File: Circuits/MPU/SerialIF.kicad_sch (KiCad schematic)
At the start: 16 parts, among them U1 ProASIC, U2 ADM3488ARZ, X1 KC2016K50.0000C1GE00

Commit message: MXS interface
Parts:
- added R222: 249, Resistor_SMD:R_0603_1608Metric, symbol QuERI_symbols:Rlowp
- U1: footprint Package_BGA:BGA-484_23.0x23.0mm_Layout22x22_P1.0mm -> Package_BGA:BGA-484_23.0x23.0mm_Layout22x22_P1.0mm
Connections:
- new net: R222.1, U1.P4 (MXAD)
- new net MXAD: R222.2
- new net MXAS: U1.N5 (MXAS)
- new net MXCLK: U1.N6 (MXCLK)
- new net MXDD: U1.M3 (MXDD)
- new net MXDS: U1.M7 (MXDS)

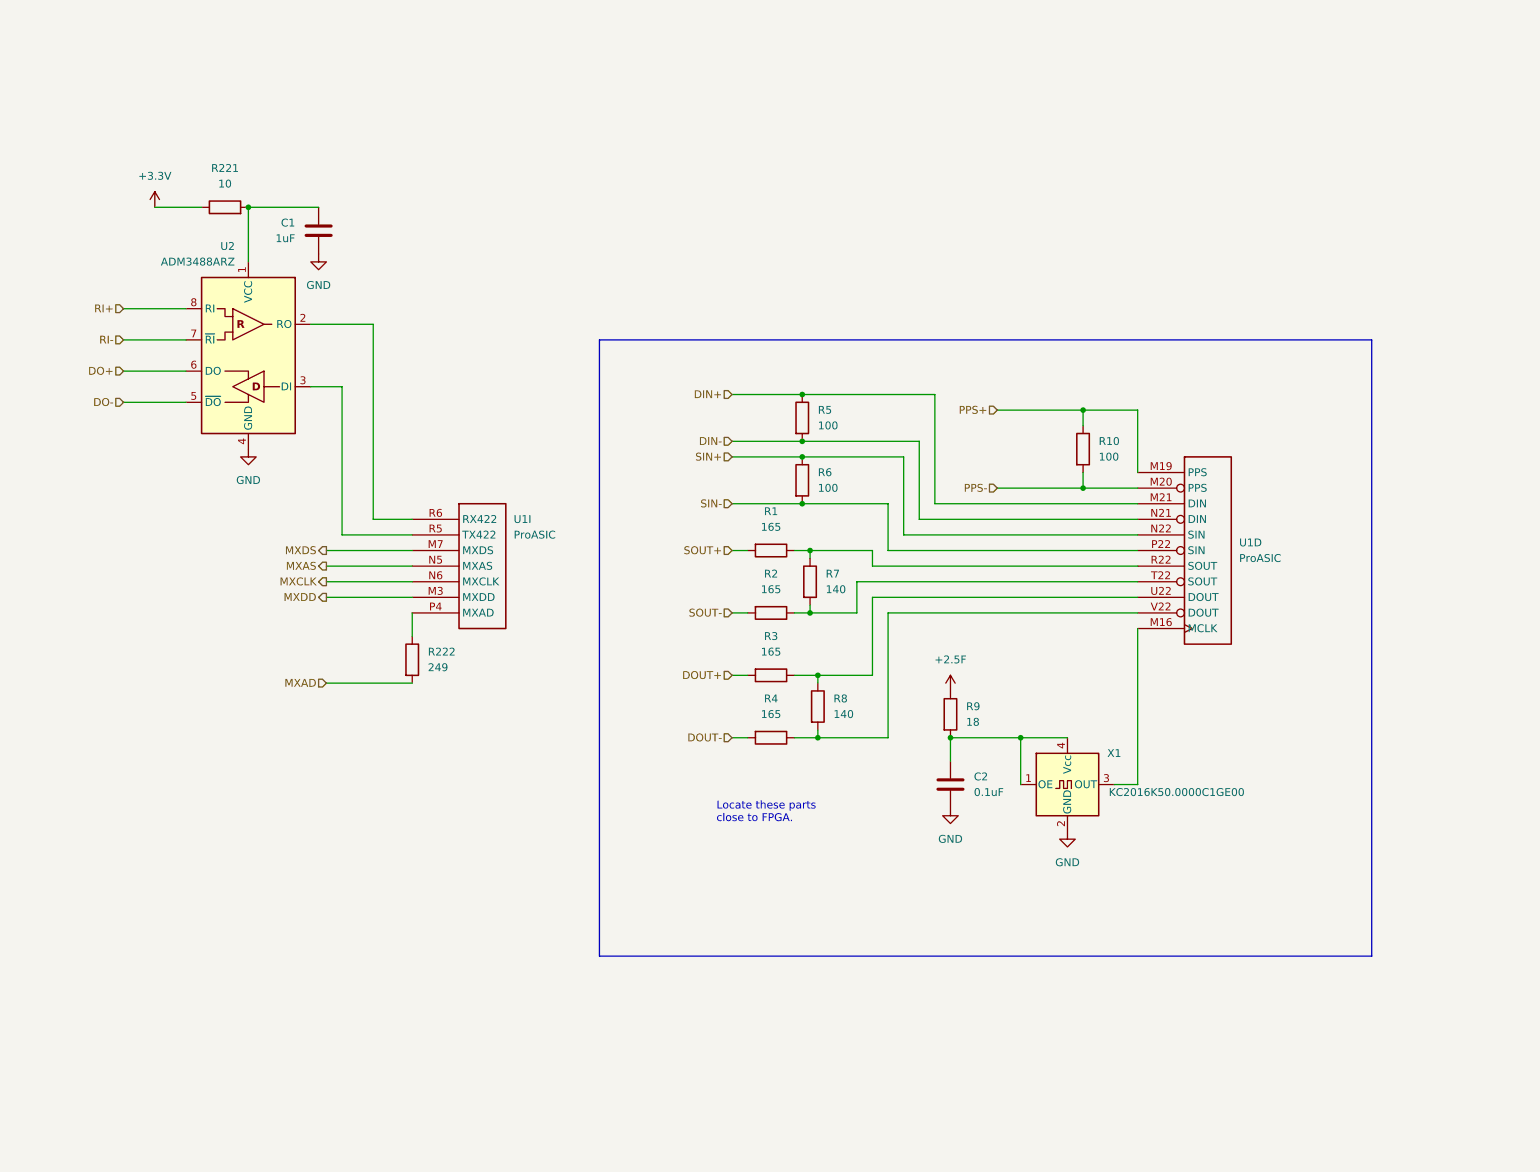
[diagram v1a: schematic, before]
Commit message: LVDS I/F for HV
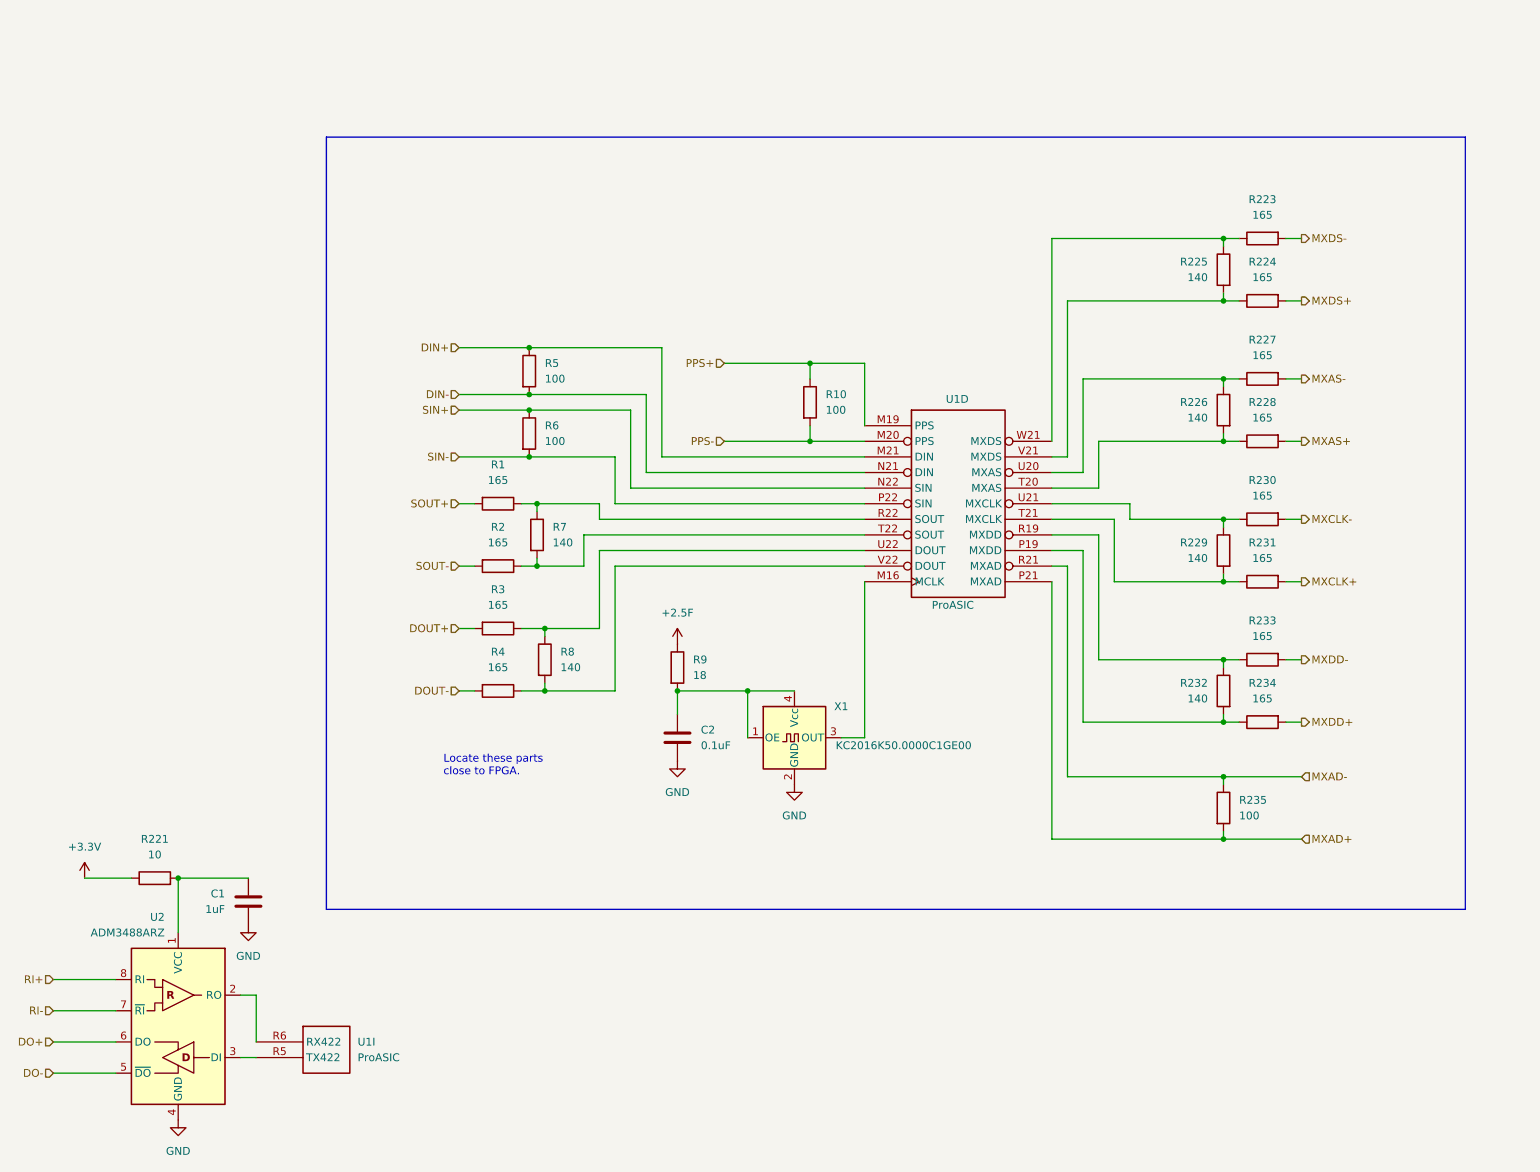
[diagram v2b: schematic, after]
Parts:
- removed R222: 249, Resistor_SMD:R_0603_1608Metric, symbol QuERI_symbols:Rlowp
- added R223, R224, R227, R228, R230, R231, R233, R234: 165, Resistor_SMD:R_0603_1608Metric, symbol QuERI_symbols:Rlowp
- added R225, R226, R229, R232: 140, Resistor_SMD:R_0603_1608Metric, symbol QuERI_symbols:Rlowp
- added R235: 100, Resistor_SMD:R_0603_1608Metric, symbol QuERI_symbols:Rlowp
- U1: desc FPGA -> FPGA; manf# A3PE3000-FGG484 -> A3PE3000-FGG484
- U1: footprint Package_BGA:BGA-484_23.0x23.0mm_Layout22x22_P1.0mm -> Package_BGA:BGA-484_23.0x23.0mm_Layout22x22_P1.0mm; desc FPGA -> FPGA; manf# (none) -> A3PE3000-FGG484
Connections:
- removed net MXAS: U1.N5 (MXAS)
- removed net MXCLK: U1.N6 (MXCLK)
- removed net MXDD: U1.M3 (MXDD)
- removed net MXDS: U1.M7 (MXDS)
- new net: R226.1, R227.1, U1.U20 (MXAS)
- new net: R224.1, R225.2, U1.V21 (MXDS)
- new net: R229.1, R230.1, U1.U21 (MXCLK)
- new net: R229.2, R231.1, U1.T21 (MXCLK)
- new net: R232.1, R233.1, U1.R19 (MXDD)
- new net: R232.2, R234.1, U1.P19 (MXDD)
- new net: R226.2, R228.1, U1.T20 (MXAS)
- new net: R223.1, R225.1, U1.W21 (MXDS)
- new net MXAD+: R235.2, U1.P21 (MXAD)
- new net MXAD-: R235.1, U1.R21 (MXAD)
- new net MXAS+: R228.2
- new net MXAS-: R227.2
- new net MXCLK+: R231.2
- new net MXCLK-: R230.2
- new net MXDD+: R234.2
- new net MXDD-: R233.2
- new net MXDS+: R224.2
- new net MXDS-: R223.2
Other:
- moved on the sheet: C1, C2, R1, R10, R2, R221, R3, R4, R5, R6, R7, R8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

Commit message: PPS is RS422, add MXINH
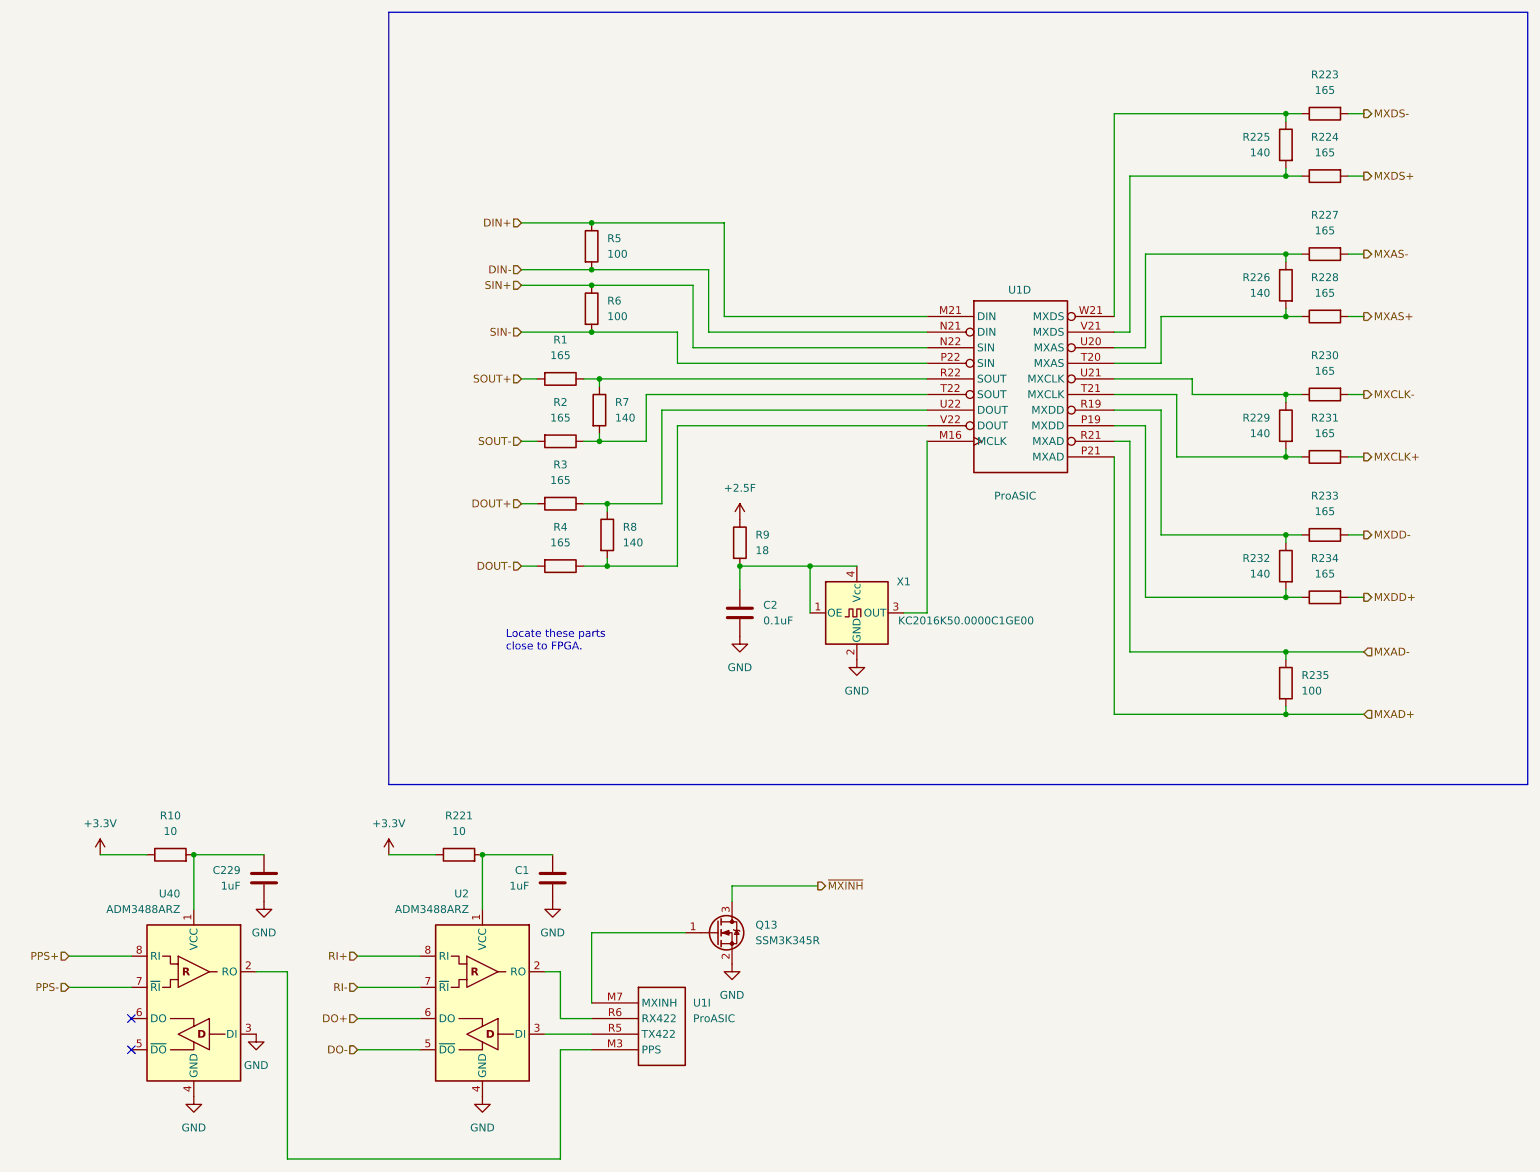
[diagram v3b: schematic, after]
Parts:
- removed R10: 100, Resistor_SMD:R_0603_1608Metric, symbol QuERI_symbols:Rlowp
- added C229: 1uF, Capacitor_SMD:C_0805_2012Metric, symbol QuERI_symbols:C
- added Q13: SSM3K345R, Package_TO_SOT_SMD:SOT-23, symbol QuERI_symbols:SSM3K345R
- added R10: 10, Resistor_SMD:R_2512_6332Metric, symbol Device:R
- added U40: ADM3488ARZ, Package_SO:SOIC-8_3.9x4.9mm_P1.27mm, symbol Interface_LineDriver:DS89C21
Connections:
- net +3.3V: now also R10.1
- net GND: now also C229.2, Q13.2 (S), U40.3 (DI), U40.4 (GND)
- net PPS+: now also U40.8 (RI); no longer U1.M19 (PPS)
- net PPS-: now also U40.7 (~{RI}); no longer U1.M20 (PPS)
- new net: U1.M3 (PPS), U40.2 (RO)
- new net: Q13.1 (G), U1.M7 (MXINH)
- new net: C229.1, R10.2, U40.1 (VCC)
- new net ~{MXINH}: Q13.3 (D)
- no-connect marks 0 -> 2
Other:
- moved on the sheet: C1, C2, R1, R2, R221, R223, R224, R225, R226, R227, R228, R229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
